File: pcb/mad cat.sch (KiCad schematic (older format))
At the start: 245 parts, among them J1 Conn_01x04, J2 Conn_02x03_Odd_Even, SW0,0 ESC, SW0,1 ESC/F1, SW0,10 F9, SW0,10-1 F10, SW0,11 F10, SW0,11-1 F11, SW0,12 F11, SW0,12-1 F12, SW0,13 F12/PRT, SW0,14 INS, SW0,15 HOME, SW0,16 PGUP, SW0,2 F1, SW0,2-1 F2, SW0,3 F2, SW0,3-1 F3, SW0,4 F3, SW0,4-1 F4, SW0,5 F4, SW0,5-1 F5, SW0,6 F5, SW0,6-1 F6, SW0,7 F6, SW0,7-1 F7, SW0,8 F7, SW0,8-1 F8, SW0,9 F8, SW0,9-1 F9, SW1,0 PF1, SW1,1 TILDE, SW1,10 9, SW1,11 0, SW1,12 -, SW1,13 =, SW1,14 BACKSPACE, SW1,14-1 S_BS_L, SW1,15 END, SW1,16 PGDN, SW1,2 1, SW1,3 2, SW1,4 3, SW1,5 4, SW1,6 5, SW1,7 6, SW1,8 7, SW1,9 8, SW2,0 PF2, SW2,1 TAB, SW2,10 O, SW2,11 P, SW2,12 [, SW2,13 ], SW2,14 \\, SW2,15 S_BS_R, SW2,16 PRT, SW2,2 Q, SW2,3 W, SW2,4 E, SW2,5 R, SW2,6 T, SW2,7 Y, SW2,8 U, SW2,9 I, SW3,0 PF3, SW3,1 CAPS, SW3,1-1 ST_CAPS, SW3,10 L, SW3,11 COLONS, SW3,12 QUOTE, SW3,13 ISO_#, SW3,14 ENT, SW3,14-1 ISO_ENT, SW3,15 DEL, SW3,16 NP_ENT, SW3,16-1 1U_ENT, SW3,2 A, SW3,3 S, SW3,4 D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

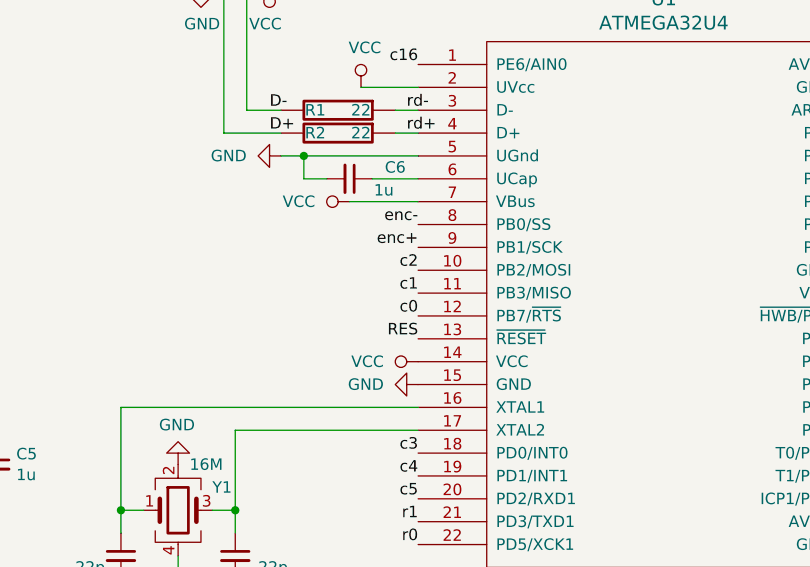
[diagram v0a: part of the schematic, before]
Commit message: adding flex cuts
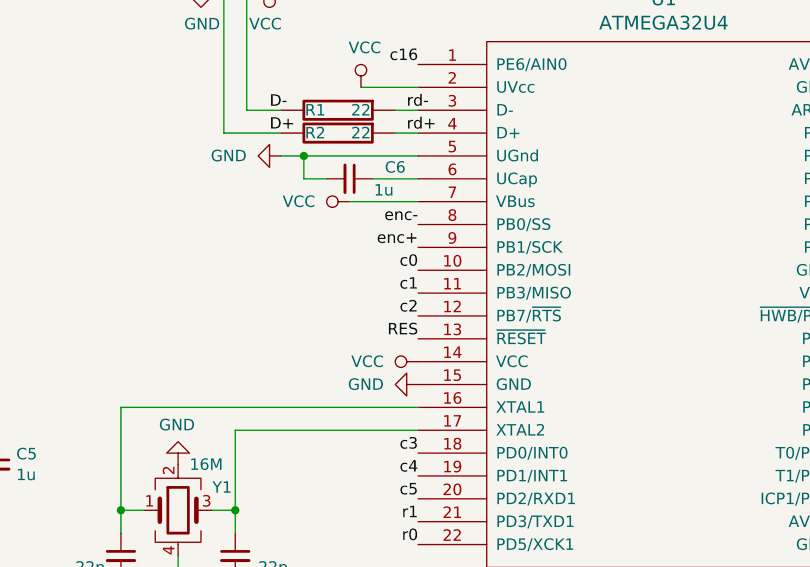
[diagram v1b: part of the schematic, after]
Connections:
- net c0: now also U1.10 (PB2/MOSI); no longer U1.12 (PB7/~RTS)
- net c2: now also U1.12 (PB7/~RTS); no longer U1.10 (PB2/MOSI)
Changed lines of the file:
@@
 	0    1    1    0
 $EndComp
-Text Label 5400 7300 2    50   ~ 0
+Text Label 5400 7100 2    50   ~ 0
 c0
 Text Label 5400 7200 2    50   ~ 0
 c1
-Text Label 5400 7100 2    50   ~ 0
+Text Label 5400 7300 2    50   ~ 0
 c2
 Text Label 5400 7900 2    50   ~ 0

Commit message: updating pcb cuts
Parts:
- SW5,7: footprint MX_SMK_2:MX_SMK_600 -> MX_SMK_2:MX_SMK_600_stabflip
- SW5,7-1: footprint MX_SMK_2:MX_SMK_625_stabflip -> MX_SMK_2:MX_SMK_625
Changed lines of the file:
@@
 EESchema Schematic File Version 4
+LIBS:mad cat-cache
 EELAYER 29 0
 EELAYER END
@@
 F 0 "SW5,7" H 6300 4200 50  0000 C CNN
 F 1 "6 SPACE" H 6300 3950 50  0000 C CNN
-F 2 "MX_SMK_2:MX_SMK_600" H 6300 4050 60  0001 C CNN
+F 2 "MX_SMK_2:MX_SMK_600_stabflip" H 6300 4050 60  0001 C CNN
 F 3 "" H 6300 4050 60  0000 C CNN
 	1    6300 4050
@@
 F 0 "SW5,7-1" H 6300 4100 50  0000 C CNN
 F 1 "6.25 SPACE" H 6300 3850 50  0000 C CNN
-F 2 "MX_SMK_2:MX_SMK_625_stabflip" H 6300 3950 60  0001 C CNN
+F 2 "MX_SMK_2:MX_SMK_625" H 6300 3950 60  0001 C CNN
 F 3 "" H 6300 3950 60  0000 C CNN
 	1    6300 3950

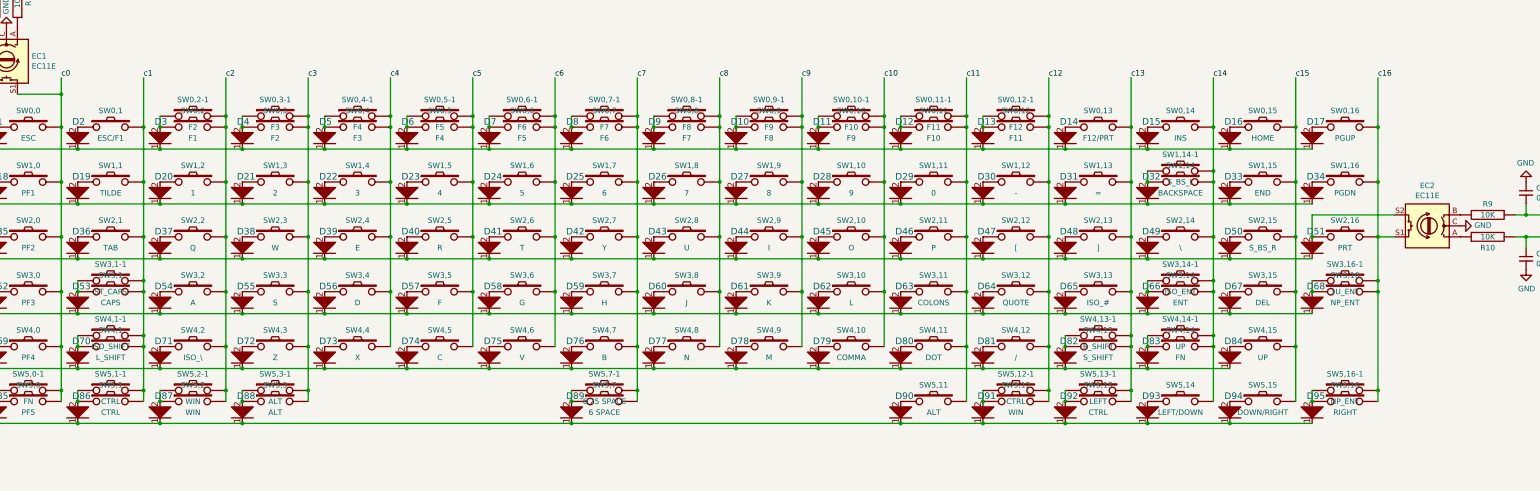
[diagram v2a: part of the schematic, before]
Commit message: rebuilding pcb, adding switches to schematic
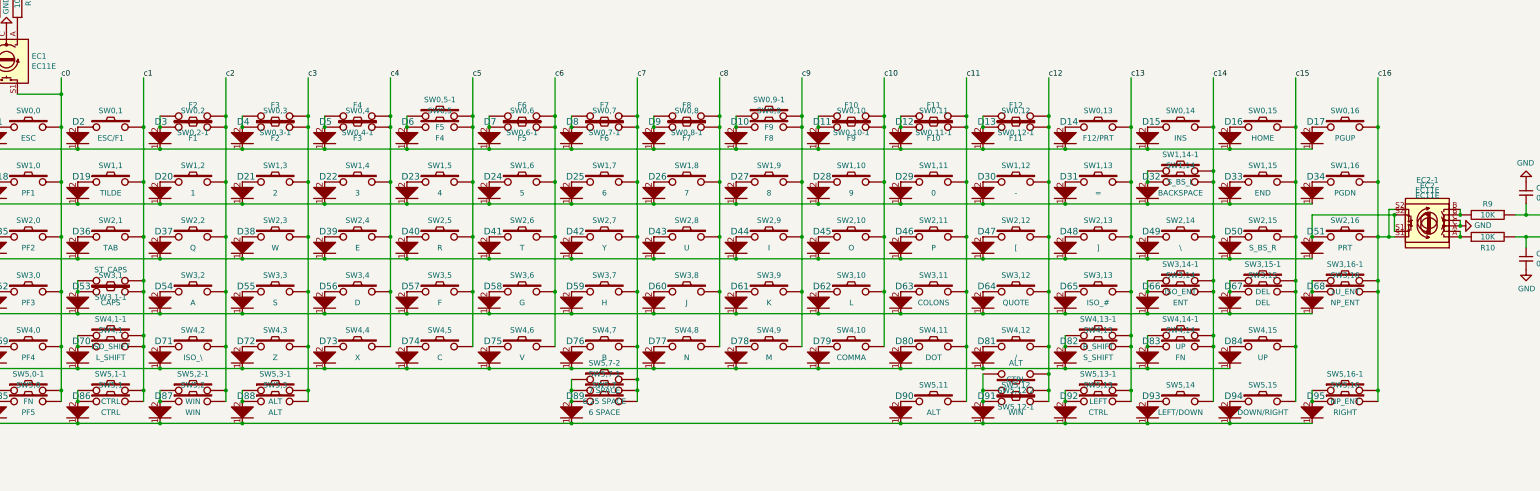
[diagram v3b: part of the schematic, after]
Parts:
- added EC2-1: EC11E, keebs:EC11E, symbol Device:Rotary_Encoder_Switch
- added SW3,15-1: DEL, MX_SMK_2:MX_SMK_200, symbol keyboard_parts:SW_PUSH
- added SW5,12-2: ALT, MX_SMK_2:MX_SMK_150, symbol keyboard_parts:SW_PUSH
- added SW5,7-2: 7 SPACE, MX_SMK_2:MX_SMK_700_stabflip, symbol keyboard_parts:SW_PUSH
- C1, C10, C11, C12, C13, C2, C3, C4, C5, C6, C7, C8, C9: footprint Capacitor_SMD:C_0805_2012Metric -> Capacitor_SMD:C_0603_1608Metric
- R1, R10, R2, R5, R6, R7, R8, R9: footprint Resistor_SMD:R_0805_2012Metric -> Resistor_SMD:R_0603_1608Metric
- SW5,7-1: footprint MX_SMK_2:MX_SMK_625 -> MX_SMK_2:MX_SMK_625_stabflip
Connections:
- net GND: now also EC2-1.C
- net c1: now also SW3,1-1.1; no longer SW3,1-1.2
- net c10: now also SW0,10-1.1; no longer SW0,10-1.2
- net c11: now also SW0,11-1.1; no longer SW0,11-1.2
- net c12: now also SW0,12-1.1, SW5,12-1.1, SW5,12-2.1; no longer SW0,12-1.2, SW5,12-1.2
- net c15: now also SW3,15-1.2
- net c16: now also EC2-1.S2
- net c2: now also SW0,2-1.1; no longer SW0,2-1.2
- net c3: now also SW0,3-1.1; no longer SW0,3-1.2
- net c4: now also SW0,4-1.1; no longer SW0,4-1.2
- net c6: now also SW0,6-1.1; no longer SW0,6-1.2
- net c7: now also SW0,7-1.1, SW5,7-2.2; no longer SW0,7-1.2
- net c8: now also SW0,8-1.1; no longer SW0,8-1.2
- net at EC2.A, R10.1: now also EC2-1.A
- net at EC2.B, R9.2: now also EC2-1.B
- net at D51.2, EC2.S2, SW2,16.1: now also EC2-1.S1
- net at D53.2, SW3,1.1: now also SW3,1-1.2; no longer SW3,1-1.1
- net at D3.2, SW0,2.1: now also SW0,2-1.2; no longer SW0,2-1.1
- net at D4.2, SW0,3.1: now also SW0,3-1.2; no longer SW0,3-1.1
- net at D5.2, SW0,4.1: now also SW0,4-1.2; no longer SW0,4-1.1
- net at D7.2, SW0,6.1: now also SW0,6-1.2; no longer SW0,6-1.1
- net at D8.2, SW0,7.1: now also SW0,7-1.2; no longer SW0,7-1.1
- net at D89.2, SW5,7-1.1, SW5,7.1: now also SW5,7-2.1
- net at D9.2, SW0,8.1: now also SW0,8-1.2; no longer SW0,8-1.1
- net at D11.2, SW0,10.1: now also SW0,10-1.2; no longer SW0,10-1.1
- net at D12.2, SW0,11.1: now also SW0,11-1.2; no longer SW0,11-1.1
- net at D13.2, SW0,12.1: now also SW0,12-1.2; no longer SW0,12-1.1
- net at D91.2, SW5,12.1: now also SW5,12-1.2, SW5,12-2.2; no longer SW5,12-1.1
- net at D67.2, SW3,15.1: now also SW3,15-1.1
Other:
- moved on the sheet: SW0,10-1, SW0,11-1, SW0,12-1, SW0,2-1, SW0,3-1, SW0,4-1, SW0,6-1, SW0,7-1, SW0,8-1, SW3,1-1, SW5,12-1

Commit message: even more compat, generating gerbers
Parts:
- added SW5,2-2: ALT, MX_SMK_2:MX_SMK_150, symbol keyboard_parts:SW_PUSH
- added SW5,7-3: 7 SPACE, MX_SMK_2:MX_SMK_700_stabflip, symbol keyboard_parts:SW_PUSH
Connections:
- net c2: now also SW5,2-2.1
- net c7: now also SW5,7-3.1
- net at D87.2, SW5,2-1.1, SW5,2.1: now also SW5,2-2.2
- net at D89.2, SW5,7-1.1, SW5,7-2.1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: now also SW5,7-3.2
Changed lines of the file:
@@
 Connection ~ 6600 3950
 Wire Wire Line
-	6600 3950 6600 3850
+	6600 3950 6600 3900
 Wire Wire Line
 	6000 3950 6000 4050
@@
 Connection ~ 2850 3950
 Wire Wire Line
-	2850 3950 2850 3550
+	2850 3950 2850 3850
 Wire Wire Line
 	2250 3950 2250 4050
@@
 	6600 3850 6600 3550
 Wire Wire Line
-	6000 3850 6000 3950
+	6000 3850 6000 3900
 Connection ~ 6000 3950
+$Comp
+L keyboard_parts:SW_PUSH SW5,2-2
+U 1 1 5CDD1EA0
+P 2550 3850
+F 0 "SW5,2-2" H 2550 4000 50  0000 C CNN
+F 1 "ALT" H 2550 3750 50  0000 C CNN
+F 2 "MX_SMK_2:MX_SMK_150" H 2550 3850 60  0001 C CNN
+F 3 "" H 2550 3850 60  0000 C CNN
+	1    2550 3850
+	-1   0    0    1
+$EndComp
+Connection ~ 2850 3850
+Wire Wire Line
+	2850 3850 2850 3550
+Wire Wire Line
+	2250 3850 2250 3950
+Connection ~ 2250 3950
+$Comp
+L keyboard_parts:SW_PUSH SW5,7-3
+U 1 1 5CDF148D
+P 6300 3900
+F 0 "SW5,7-3" H 6300 4050 50  0000 C CNN
+F 1 "7 SPACE" H 6300 3800 50  0000 C CNN
+F 2 "MX_SMK_2:MX_SMK_700_stabflip" H 6300 3900 60  0001 C CNN
+F 3 "" H 6300 3900 60  0000 C CNN
+	1    6300 3900
+	-1   0    0    1
+$EndComp
+Connection ~ 6600 3900
+Wire Wire Line
+	6600 3900 6600 3850
+Connection ~ 6000 3900
+Wire Wire Line
+	6000 3900 6000 3950
 $EndSCHEMATC

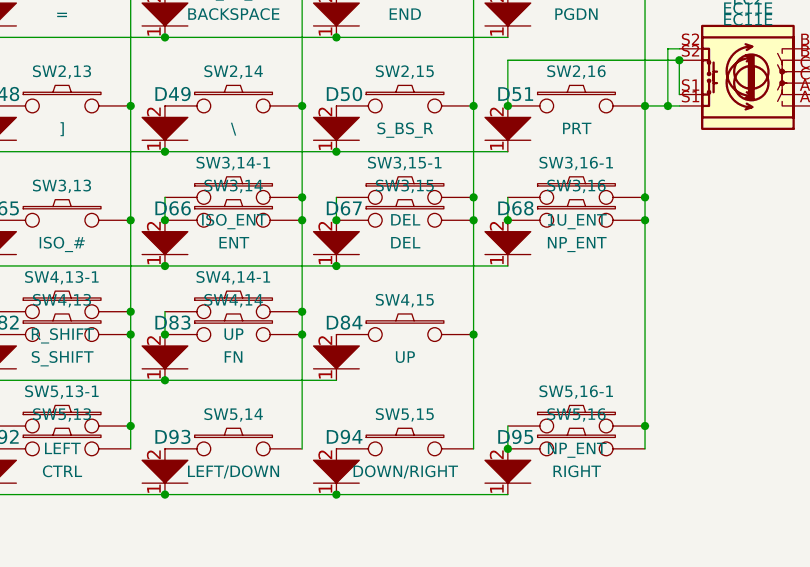
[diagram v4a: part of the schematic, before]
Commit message: new flex cuts
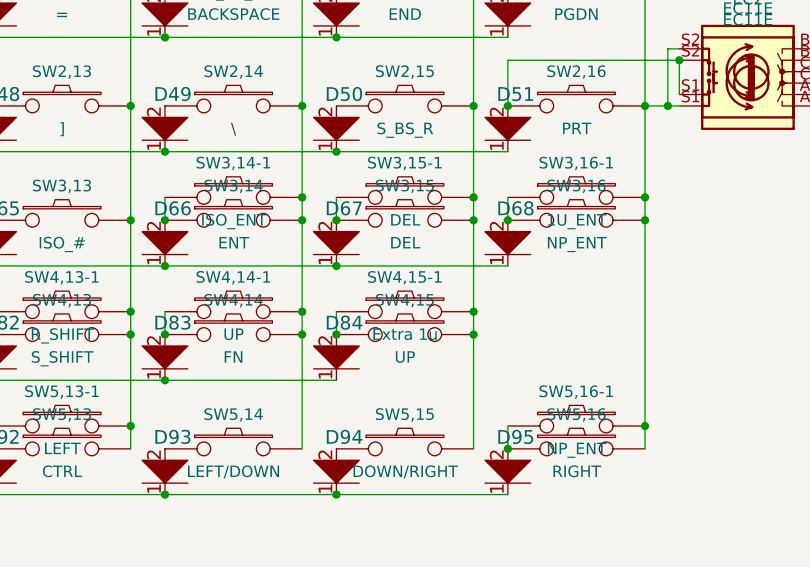
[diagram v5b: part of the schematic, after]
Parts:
- added SW4,15-1: Extra 1u, MX_SMK_2:MX_SMK_100, symbol keyboard_parts:SW_PUSH
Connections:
- net c15: now also SW4,15-1.2
- net at D84.2, SW4,15.1: now also SW4,15-1.1
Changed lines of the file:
@@
 Connection ~ 12600 3550
 Wire Wire Line
-	12600 3550 12600 3050
+	12600 3550 12600 3450
 $Comp
 L keyboard_parts:SW_PUSH SW0,16
@@
 Wire Wire Line
 	6000 3900 6000 3950
+$Comp
+L keyboard_parts:SW_PUSH SW4,15-1
+U 1 1 5CE61825
+P 12300 3450
+F 0 "SW4,15-1" H 12300 3600 50  0000 C CNN
+F 1 "Extra 1u" H 12300 3350 50  0000 C CNN
+F 2 "MX_SMK_2:MX_SMK_100" H 12300 3450 60  0001 C CNN
+F 3 "" H 12300 3450 60  0000 C CNN
+	1    12300 3450
+	1    0    0    -1
+$EndComp
+Connection ~ 12600 3450
+Wire Wire Line
+	12600 3450 12600 3050
+Wire Wire Line
+	12000 3450 12000 3550
+Connection ~ 12000 3550
 $EndSCHEMATC

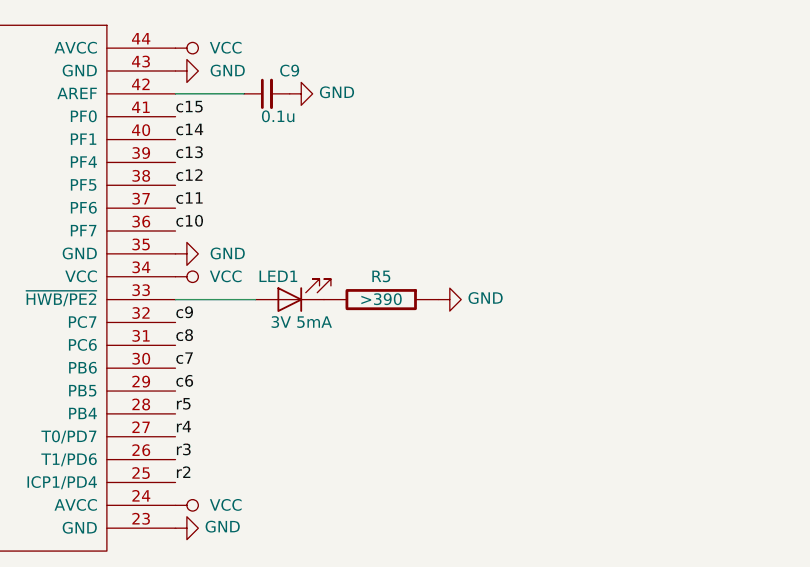
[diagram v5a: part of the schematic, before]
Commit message: redoing in mx only, adding trimpot for led
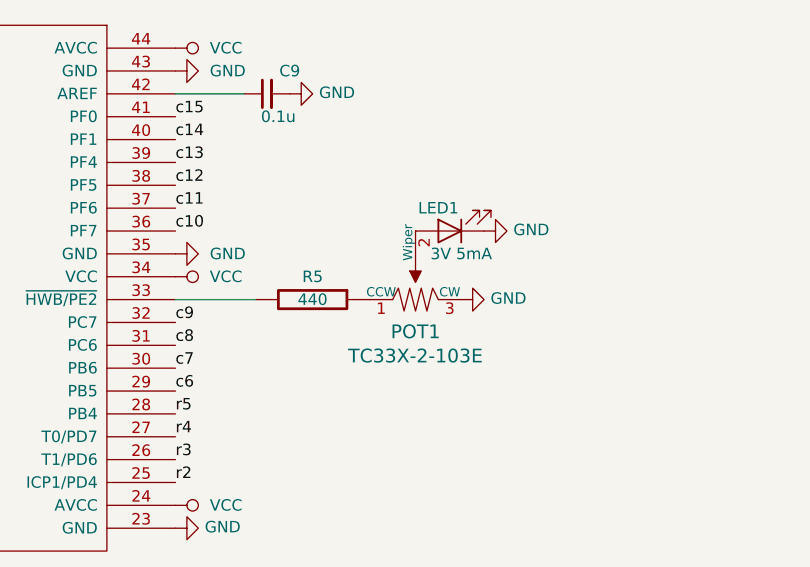
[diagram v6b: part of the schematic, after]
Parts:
- added POT1: TC33X-2-103E, digikey-footprints:Trimpot_3.8mmx3.6mm_TC33X-2-103E, symbol dk_Trimmer-Potentiometers:TC33X-2-103E
- LED1: footprint keebs:LED_D1.8mm_W3.3mm_H2.4mm_CENTERED -> keebs:LED_0805_lightpipe
- R5: value >390 -> 440
- SW0,0, SW0,1, SW0,10, SW0,10-1, SW0,11, SW0,11-1, SW0,12, SW0,12-1, SW0,13, SW0,14, SW0,15, SW0,16, SW0,2, SW0,2-1, SW0,3, SW0,3-1, SW0,4, SW0,4-1, SW0,5, SW0,5-1, SW0,6, SW0,6-1, SW0,7, SW0,7-1, SW0,8, SW0,8-1, SW0,9, SW0,9-1, SW1,0, SW1,1, SW1,10, SW1,11, SW1,12, SW1,13, SW1,14-1, SW1,15, SW1,16, SW1,2, SW1,3, SW1,4, SW1,5, SW1,6, SW1,7, SW1,8, SW1,9, SW2,0, SW2,10, SW2,11, SW2,12, SW2,13, SW2,15, SW2,16, SW2,2, SW2,3, SW2,4, SW2,5, SW2,6, SW2,7, SW2,8, SW2,9, SW3,0, SW3,10, SW3,11, SW3,12, SW3,13, SW3,16-1, SW3,2, SW3,3, SW3,4, SW3,5, SW3,6, SW3,7, SW3,8, SW3,9, SW4,0, SW4,10, SW4,11, SW4,12, SW4,14, SW4,14-1, SW4,15, SW4,15-1, SW4,2, SW4,3, SW4,4, SW4,5, SW4,6, SW4,7, SW4,8, SW4,9, SW5,0, SW5,0-1, SW5,12, SW5,13-1, SW5,14, SW5,15, SW5,16, SW5,2: footprint MX_SMK_2:MX_SMK_100 -> MX_SMK_2:MX_100
- SW1,14, SW3,15, SW3,15-1, SW3,16, SW5,16-1: footprint MX_SMK_2:MX_SMK_200 -> MX_SMK_2:MX_200
- SW2,1, SW2,14, SW5,1, SW5,11, SW5,12-1, SW5,12-2, SW5,13, SW5,2-2, SW5,3: footprint MX_SMK_2:MX_SMK_150 -> MX_SMK_2:MX_150
- SW3,1, SW4,13: footprint MX_SMK_2:MX_SMK_175 -> MX_SMK_2:MX_175
- SW3,1-1, SW4,1-1, SW5,1-1, SW5,2-1, SW5,3-1: footprint MX_SMK_2:MX_SMK_125 -> MX_SMK_2:MX_125
- SW3,14, SW4,1: footprint MX_SMK_2:MX_SMK_225 -> MX_SMK_2:MX_225
- SW3,14-1: footprint MX_SMK_2:MX_SMK_ISO_stabflip -> MX_SMK_2:MX_ISO_stabflip
- SW4,13-1: footprint MX_SMK_2:MX_SMK_275 -> MX_SMK_2:MX_275
- SW5,7: footprint MX_SMK_2:MX_SMK_600_stabflip -> MX_SMK_2:MX_600_stabflip
- SW5,7-1: footprint MX_SMK_2:MX_SMK_625_stabflip -> MX_SMK_2:MX_625_stabflip
- SW5,7-2, SW5,7-3: footprint MX_SMK_2:MX_SMK_700_stabflip -> MX_SMK_2:MX_700_stabflip
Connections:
- net GND: now also LED1.1 (K), POT1.3 (CW); no longer R5.1
- net at U1.33 (~HWB/PE2): now also R5.2; no longer LED1.2 (A)
- new net: LED1.2 (A), POT1.2 (Wiper)
- new net: POT1.1 (CCW), R5.1
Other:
- moved on the sheet: LED1, R5

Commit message: fixed silk, created gerbers
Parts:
- added SW1,0-1: PF1, MX_SMK_2:MX_100, symbol keyboard_parts:SW_PUSH
- added SW2,0-1: PF2, MX_SMK_2:MX_100, symbol keyboard_parts:SW_PUSH
- added SW3,0-1: PF3, MX_SMK_2:MX_100, symbol keyboard_parts:SW_PUSH
- added SW4,0-1: PF4, MX_SMK_2:MX_100, symbol keyboard_parts:SW_PUSH
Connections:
- net c0: now also SW1,0-1.2, SW2,0-1.2, SW3,0-1.2, SW4,0-1.2
- net at D18.2, SW1,0.1: now also SW1,0-1.1
- net at D35.2, SW2,0.1: now also SW2,0-1.1
- net at D52.2, SW3,0.1: now also SW3,0-1.1
- net at D69.2, SW4,0.1: now also SW4,0-1.1
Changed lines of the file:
@@
 Connection ~ 1350 2050
 Wire Wire Line
-	1350 2050 1350 1550
+	1350 2050 1350 1950
 Connection ~ 1350 2550
 Wire Wire Line
-	1350 2550 1350 2050
+	1350 2550 1350 2450
 Connection ~ 1350 3050
 Wire Wire Line
-	1350 3050 1350 2550
+	1350 3050 1350 2950
 Connection ~ 1350 3550
 Wire Wire Line
-	1350 3550 1350 3050
+	1350 3550 1350 3450
 $Comp
 L keyboard_parts:SW_PUSH SW0,1
@@
 	0    -1   -1   0
 $EndComp
+$Comp
+L keyboard_parts:SW_PUSH SW4,0-1
+U 1 1 5D035F35
+P 1050 3450
+F 0 "SW4,0-1" H 1050 3600 50  0000 C CNN
+F 1 "PF4" H 1050 3350 50  0000 C CNN
+F 2 "MX_SMK_2:MX_100" H 1050 3450 60  0001 C CNN
+F 3 "" H 1050 3450 60  0000 C CNN
+	1    1050 3450
+	1    0    0    -1
+$EndComp
+Connection ~ 1350 3450
+Wire Wire Line
+	1350 3450 1350 3050
+Wire Wire Line
+	750  3450 750  3550
+Connection ~ 750  3550
+$Comp
+L keyboard_parts:SW_PUSH SW3,0-1
+U 1 1 5D053882
+P 1050 2950
+F 0 "SW3,0-1" H 1050 3100 50  0000 C CNN
+F 1 "PF3" H 1050 2850 50  0000 C CNN
+F 2 "MX_SMK_2:MX_100" H 1050 2950 60  0001 C CNN
+F 3 "" H 1050 2950 60  0000 C CNN
+	1    1050 2950
+	1    0    0    -1
+$EndComp
+Connection ~ 1350 2950
+Wire Wire Line
+	1350 2950 1350 2550
+Wire Wire Line
+	750  2950 750  3050
+Connection ~ 750  3050
+$Comp
+L keyboard_parts:SW_PUSH SW2,0-1
+U 1 1 5D071A92
+P 1050 2450
+F 0 "SW2,0-1" H 1050 2600 50  0000 C CNN
+F 1 "PF2" H 1050 2350 50  0000 C CNN
+F 2 "MX_SMK_2:MX_100" H 1050 2450 60  0001 C CNN
+F 3 "" H 1050 2450 60  0000 C CNN
+	1    1050 2450
+	1    0    0    -1
+$EndComp
+Connection ~ 1350 2450
+Wire Wire Line
+	1350 2450 1350 2050
+Wire Wire Line
+	750  2450 750  2550
+Connection ~ 750  2550
+$Comp
+L keyboard_parts:SW_PUSH SW1,0-1
+U 1 1 5D090607
+P 1050 1950
+F 0 "SW1,0-1" H 1050 2100 50  0000 C CNN
+F 1 "PF1" H 1050 1850 50  0000 C CNN
+F 2 "MX_SMK_2:MX_100" H 1050 1950 60  0001 C CNN
+F 3 "" H 1050 1950 60  0000 C CNN
+	1    1050 1950
+	1    0    0    -1
+$EndComp
+Connection ~ 1350 1950
+Wire Wire Line
+	1350 1950 1350 1550
+Wire Wire Line
+	750  1950 750  2050
+Connection ~ 750  2050
 $EndSCHEMATC
